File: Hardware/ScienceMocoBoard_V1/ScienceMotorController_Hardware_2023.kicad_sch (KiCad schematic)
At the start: 134 parts, among them Q1 SI4156DY, Q10 SI4156DY, Q11 SI4156DY, Q12 SI4156DY, Q13 SI4156DY, Q14 SI4156DY, Q15 SI4156DY, Q16 SI4156DY, Q2 SI4156DY, Q3 SI4156DY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

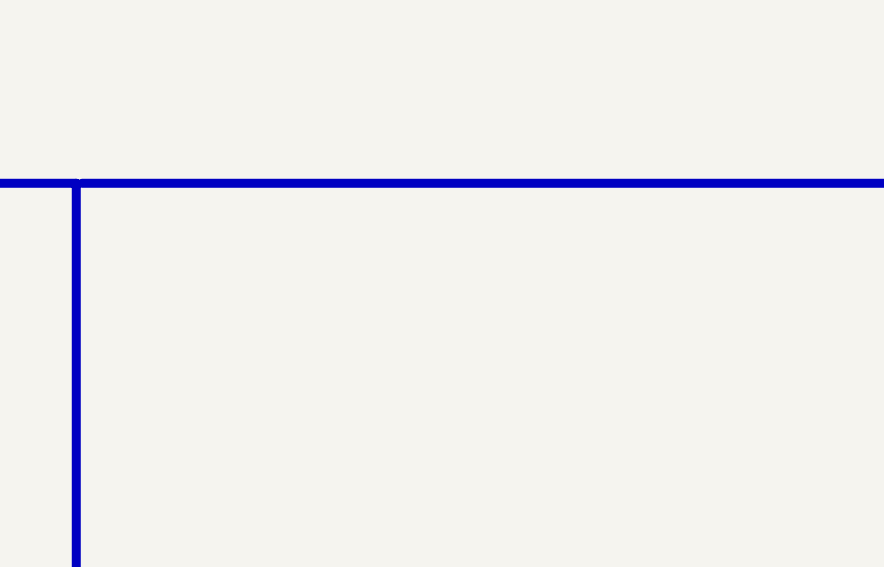
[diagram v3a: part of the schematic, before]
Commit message: Added Mounting Holes
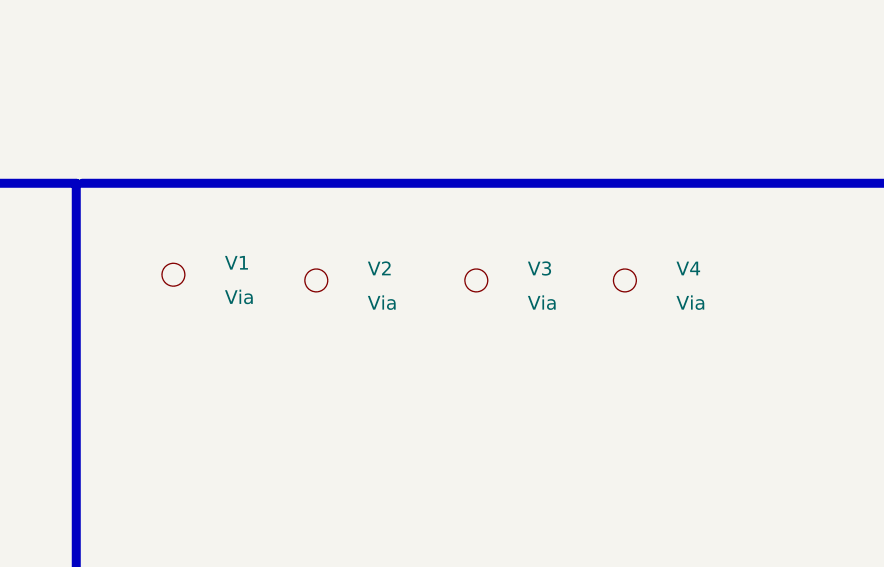
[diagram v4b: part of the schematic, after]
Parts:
- added V1, V2, V3, V4: Via, MRDT_Drill_Holes:4_40_Hole_Corner, symbol MRDT_Drill_Holes:Via
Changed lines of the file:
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@@
     (pin "8")
   )
+  (symbol (lib_id "MRDT_Drill_Holes:Via") (at 377.19 262.255 0) (unit 1)
+    (in_bom yes) (on_board yes) (fields_autoplaced)
+    (property "Reference" "V4" (id 0) (at 382.905 260.985 0)
+      (effects (font (size 1.524 1.524)) (justify left))
+    )
+    (property "Value" "Via" (id 1) (at 382.905 264.795 0)
+      (effects (font (size 1.524 1.524)) (justify left))
+    )
+    (property "Footprint" "MRDT_Drill_Holes:4_40_Hole_Corner" (id 2) (at 377.19 262.255 0)
+      (effects (font (size 1.524 1.524)) hide)
+    )
+    (property "Datasheet" "" (id 3) (at 377.19 262.255 0)
+      (effects (font (size 1.524 1.524)) hide)
+    )
+    (pin "1")
+  )
   (symbol (lib_id "MRDT_Devices:OKI") (at 88.9 300.355 0) (unit 1)
     (in_bom yes) (on_board yes)
@@
     (pin "1")
   )
+  (symbol (lib_id "MRDT_Drill_Holes:Via") (at 327.025 261.62 0) (unit 1)
+    (in_bom yes) (on_board yes) (fields_autoplaced)
+    (property "Reference" "V1" (id 0) (at 332.74 260.35 0)
+      (effects (font (size 1.524 1.524)) (justify left))
+    )
+    (property "Value" "Via" (id 1) (at 332.74 264.16 0)
+      (effects (font (size 1.524 1.524)) (justify left))
+    )
+    (property "Footprint" "MRDT_Drill_Holes:4_40_Hole_Corner" (id 2) (at 327.025 261.62 0)
+      (effects (font (size 1.524 1.524)) hide)
+    )
+    (property "Datasheet" "" (id 3) (at 327.025 261.62 0)
+      (effects (font (size 1.524 1.524)) hide)
+    )
+    (pin "1")
+  )
   (symbol (lib_id "Device:R") (at 93.98 105.41 90) (unit 1)
     (in_bom yes) (on_board yes)
@@
     (pin "2")
   )
+  (symbol (lib_id "MRDT_Drill_Holes:Via") (at 342.9 262.255 0) (unit 1)
+    (in_bom yes) (on_board yes) (fields_autoplaced)
+    (property "Reference" "V2" (id 0) (at 348.615 260.985 0)
+      (effects (font (size 1.524 1.524)) (justify left))
+    )
+    (property "Value" "Via" (id 1) (at 348.615 264.795 0)
+      (effects (font (size 1.524 1.524)) (justify left))
+    )
+    (property "Footprint" "MRDT_Drill_Holes:4_40_Hole_Corner" (id 2) (at 342.9 262.255 0)
+      (effects (font (size 1.524 1.524)) hide)
+    )
+    (property "Datasheet" "" (id 3) (at 342.9 262.255 0)
+      (effects (font (size 1.524 1.524)) hide)
+    )
+    (pin "1")
+  )
   (symbol (lib_id "Simulation_SPICE:DIODE") (at 46.99 191.77 270) (unit 1)
     (in_bom yes) (on_board yes) (fields_autoplaced)
@@
     (pin "1")
   )
+  (symbol (lib_id "MRDT_Drill_Holes:Via") (at 360.68 262.255 0) (unit 1)
+    (in_bom yes) (on_board yes) (fields_autoplaced)
+    (property "Reference" "V3" (id 0) (at 366.395 260.985 0)
+      (effects (font (size 1.524 1.524)) (justify left))
+    )
+    (property "Value" "Via" (id 1) (at 366.395 264.795 0)
+      (effects (font (size 1.524 1.524)) (justify left))
+    )
+    (property "Footprint" "MRDT_Drill_Holes:4_40_Hole_Corner" (id 2) (at 360.68 262.255 0)
+      (effects (font (size 1.524 1.524)) hide)
+    )
+    (property "Datasheet" "" (id 3) (at 360.68 262.255 0)
+      (effects (font (size 1.524 1.524)) hide)
+    )
+    (pin "1")
+  )
   (symbol (lib_id "power:GND") (at 110.49 199.39 0) (unit 1)
     (in_bom yes) (on_board yes) (fields_autoplaced)
@@
       (reference "U11") (unit 8) (value "TM4C129E_Launchpad") (footprint "MRDT_Shields:TM4C129E_Launchpad_FULL_THT_BOTTOM")
     )
+    (path "/385e1073-e8ee-4204-8262-b68e828176b6"
+      (reference "V1") (unit 1) (value "Via") (footprint "MRDT_Drill_Holes:4_40_Hole_Corner")
+    )
+    (path "/b4dcbca0-27b8-40c0-8259-04e5ea35a88a"
+      (reference "V2") (unit 1) (value "Via") (footprint "MRDT_Drill_Holes:4_40_Hole_Corner")
+    )
+    (path "/df564af1-db08-44de-89e6-2a6bfacb7389"
+      (reference "V3") (unit 1) (value "Via") (footprint "MRDT_Drill_Holes:4_40_Hole_Corner")
+    )
+    (path "/2c35478b-bc32-43b3-89fb-253ddd3b5959"
+      (reference "V4") (unit 1) (value "Via") (footprint "MRDT_Drill_Holes:4_40_Hole_Corner")
+    )
   )

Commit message: Stuff Happened
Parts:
- C11, C12, C5, C6: value 10u -> 10uF
- R11, R16, R17, R18, R19, R32, R33, R34, R35, R36, R37, R38, R39: value 130 -> 120

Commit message: Updated to Teensy.
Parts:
- removed D24, D25: RED, LED_SMD:LED_0603_1608Metric_Pad1.05x0.95mm_HandSolder, symbol Device:LED_Small
- removed R32, R33: 120, Resistor_SMD:R_0603_1608Metric_Pad0.98x0.95mm_HandSolder, symbol Device:R
- removed U11: TM4C129E_Launchpad, MRDT_Shields:TM4C129E_Launchpad_FULL_THT_BOTTOM, symbol MRDT_Shields:TM4C129E_Launchpad
- added U11: Teensy4.1_DEV-16771, MRDT_Shields:Teensy_4_1, symbol MRDT_Shields:Teensy4.1_DEV-16771
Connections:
- new net: U11.3.3V_1 (3.3V), U11.3.3V_2 (3.3V), U11.3.3V_3 (3.3V)
- new net: U11.GND1 (GND), U11.GND2 (GND), U11.GND3 (GND), U11.GND4 (GND), U11.GND5 (GND)
- new net: U11.USB_GND1 (USB_GND), U11.USB_GND2 (USB_GND)
- no-connect marks 48 -> 0
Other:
- note added: "TEENSY"
- note removed: "Red"
- note removed: "TIVA"

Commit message: Added Ethernet. Expanded Board Temporarily
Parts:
- added C15: 0.1uF, Capacitor_SMD:C_0603_1608Metric_Pad1.08x0.95mm_HandSolder, symbol Device:C
- added D24: YELLOW, LED_SMD:LED_0603_1608Metric_Pad1.05x0.95mm_HandSolder, symbol Device:LED_Small
- added J1: RJ45_LED_Shielded, MRDT_Connectors:RJ45_Teensy, symbol Connector:RJ45_LED_Shielded
- added J2: Conn_02x03_Counter_Clockwise, Connector_PinHeader_2.00mm:PinHeader_2x03_P2.00mm_Vertical, symbol Connector_Generic:Conn_02x03_Counter_Clockwise
- added LimSwitch7: Molex_SL_02, MRDT_Connectors:MOLEX_SL_02_Vertical, symbol MRDT_Connectors:Molex_SL_02
- added R32: 120, Resistor_SMD:R_0603_1608Metric_Pad0.98x0.95mm_HandSolder, symbol Device:R
- C10, C13, C14, C2, C3, C7, C8, C9: value 0.1u -> 1uF
- renumbered LimSwitch3 to LimSwitch1, LimSwitch1 to LimSwitch2, LimSwitch2 to LimSwitch3
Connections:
- net +3V3: now also LimSwitch7.1
- net Encoder_PWM_1: now also U11.38 (A14)
- net Encoder_PWM_2: now also U11.39 (A15)
- net Encoder_PWM_3: now also U11.40 (A16)
- net Encoder_PWM_4: now also U11.41 (A17)
- net FWD_PWM_1: now also U11.1 (TX1)
- net FWD_PWM_2: now also U11.3 (LRCLK2)
- net FWD_PWM_3: now also U11.6 (OUT1D)
- net FWD_PWM_4: now also U11.8 (TX2)
- net GND: now also U11.GND1 (GND), U11.GND2 (GND), U11.GND3 (GND), U11.GND4 (GND), U11.GND5 (GND), D24.1 (K), J1.SH
- net Limit_Switch_1: now also U11.16 (A2)
- net Limit_Switch_2: now also U11.17 (A3)
- net Limit_Switch_3: now also U11.18 (A4)
- net Limit_Switch_4: now also U11.19 (A5)
- net Limit_Switch_5: now also U11.20 (A6)
- net Limit_Switch_6: now also U11.21 (A7)
- net RVS_PWM_1: now also U11.2 (OUT2)
- net RVS_PWM_2: now also U11.4 (BCLK2)
- net RVS_PWM_3: now also U11.7 (RX2)
- net RVS_PWM_4: now also U11.9 (OUT1C)
- net Servo_1: now also U11.37 (CS3)
- net Servo_2: now also U11.36 (CS2)
- net Servo_3: now also U11.12 (MISO)
- net Servo_4: now also U11.11 (MOSI)
- net Servo_5: now also U11.24 (A10)
- net Servo_6: now also U11.23 (A9)
- net Limit_Switch_7: now reaches U11.22 (A8)
- net Limit_Switch_7: now also LimSwitch7.2, R32.2
- net +3.3V: now reaches U11.3.3V_1 (3.3V), U11.3.3V_2 (3.3V), U11.3.3V_3 (3.3V)
- new net: C15.1, J1.2, J1.5
- new net: C15.2, J1.8
- new net: D24.2 (A), R32.1
- new net: J1.1, J2.1 (Pin_1)
- new net: J1.10, J2.4 (Pin_4)
- new net: J1.3, J2.2 (Pin_2)
- new net: J1.4, J2.6 (Pin_6)
- new net: J1.6, J2.5 (Pin_5)
- new net: J1.9, J2.3 (Pin_3)
- no-connect marks 0 -> 33
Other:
- note added: "Rx +"
- note added: "Rx -"
- note added: "Tx +"
- note added: "Tx -"
- note added: "Vias"
- moved on the sheet: U11, V1, V2, V3, V4

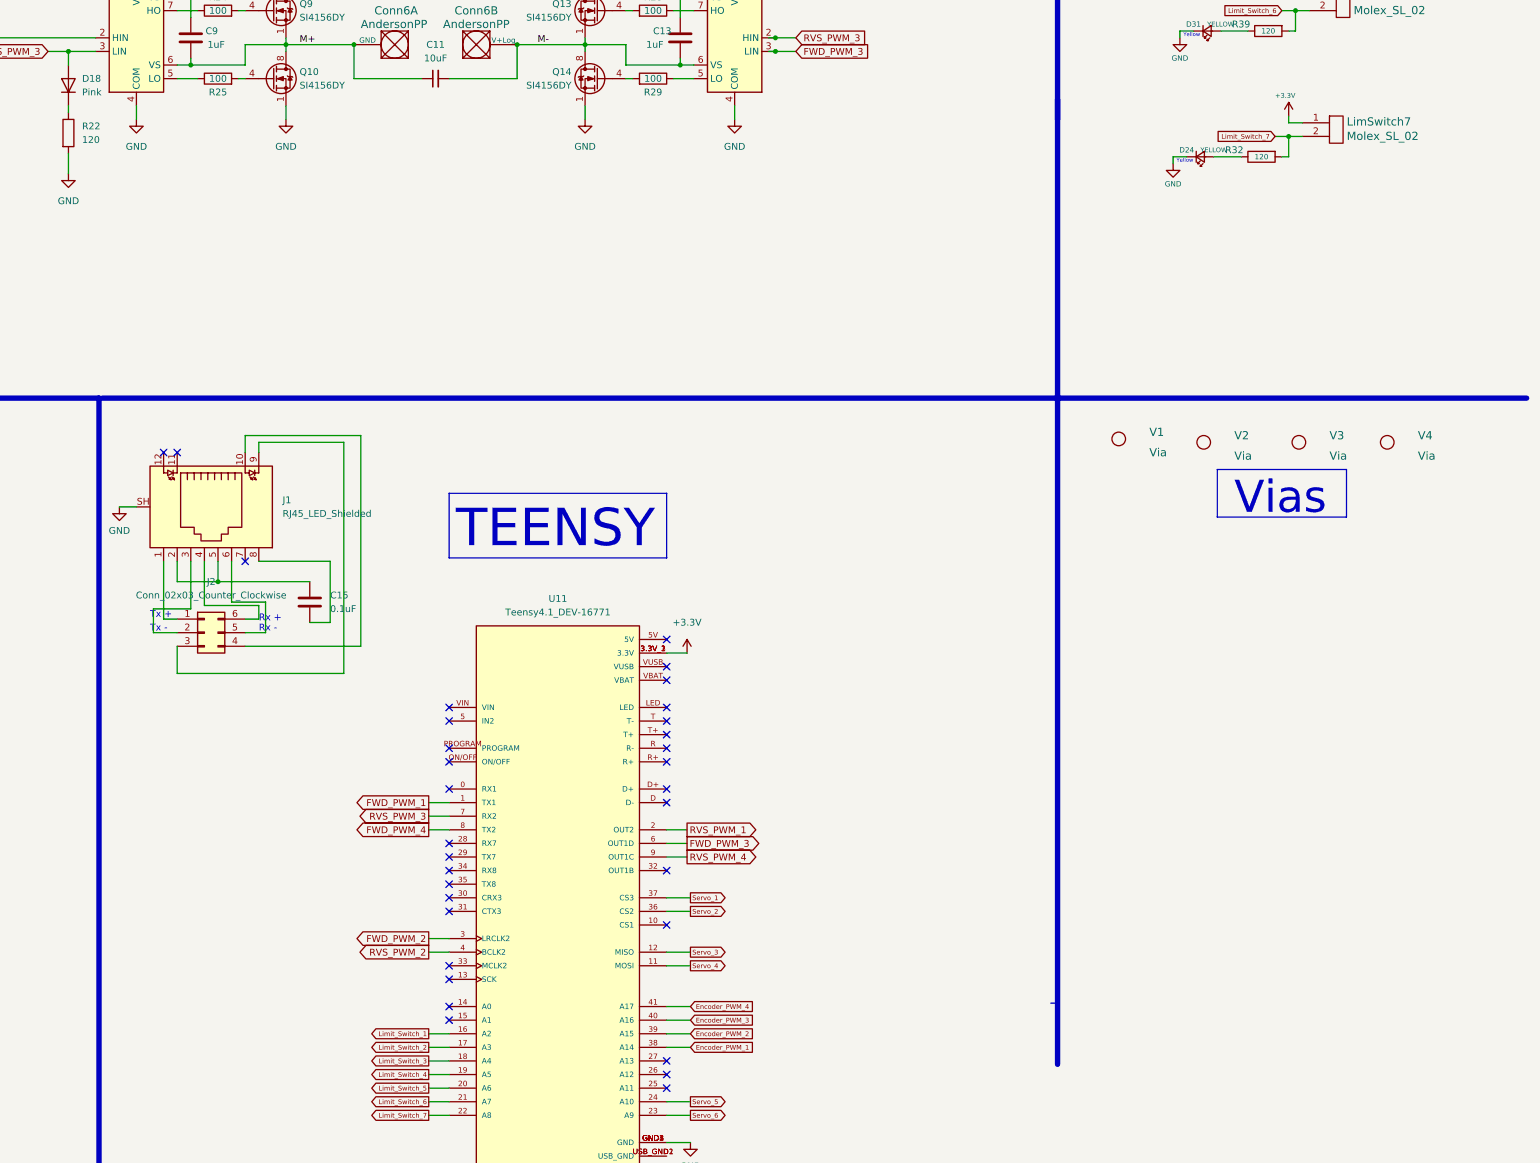
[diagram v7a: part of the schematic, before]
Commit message: Added Buttons to Schematic.
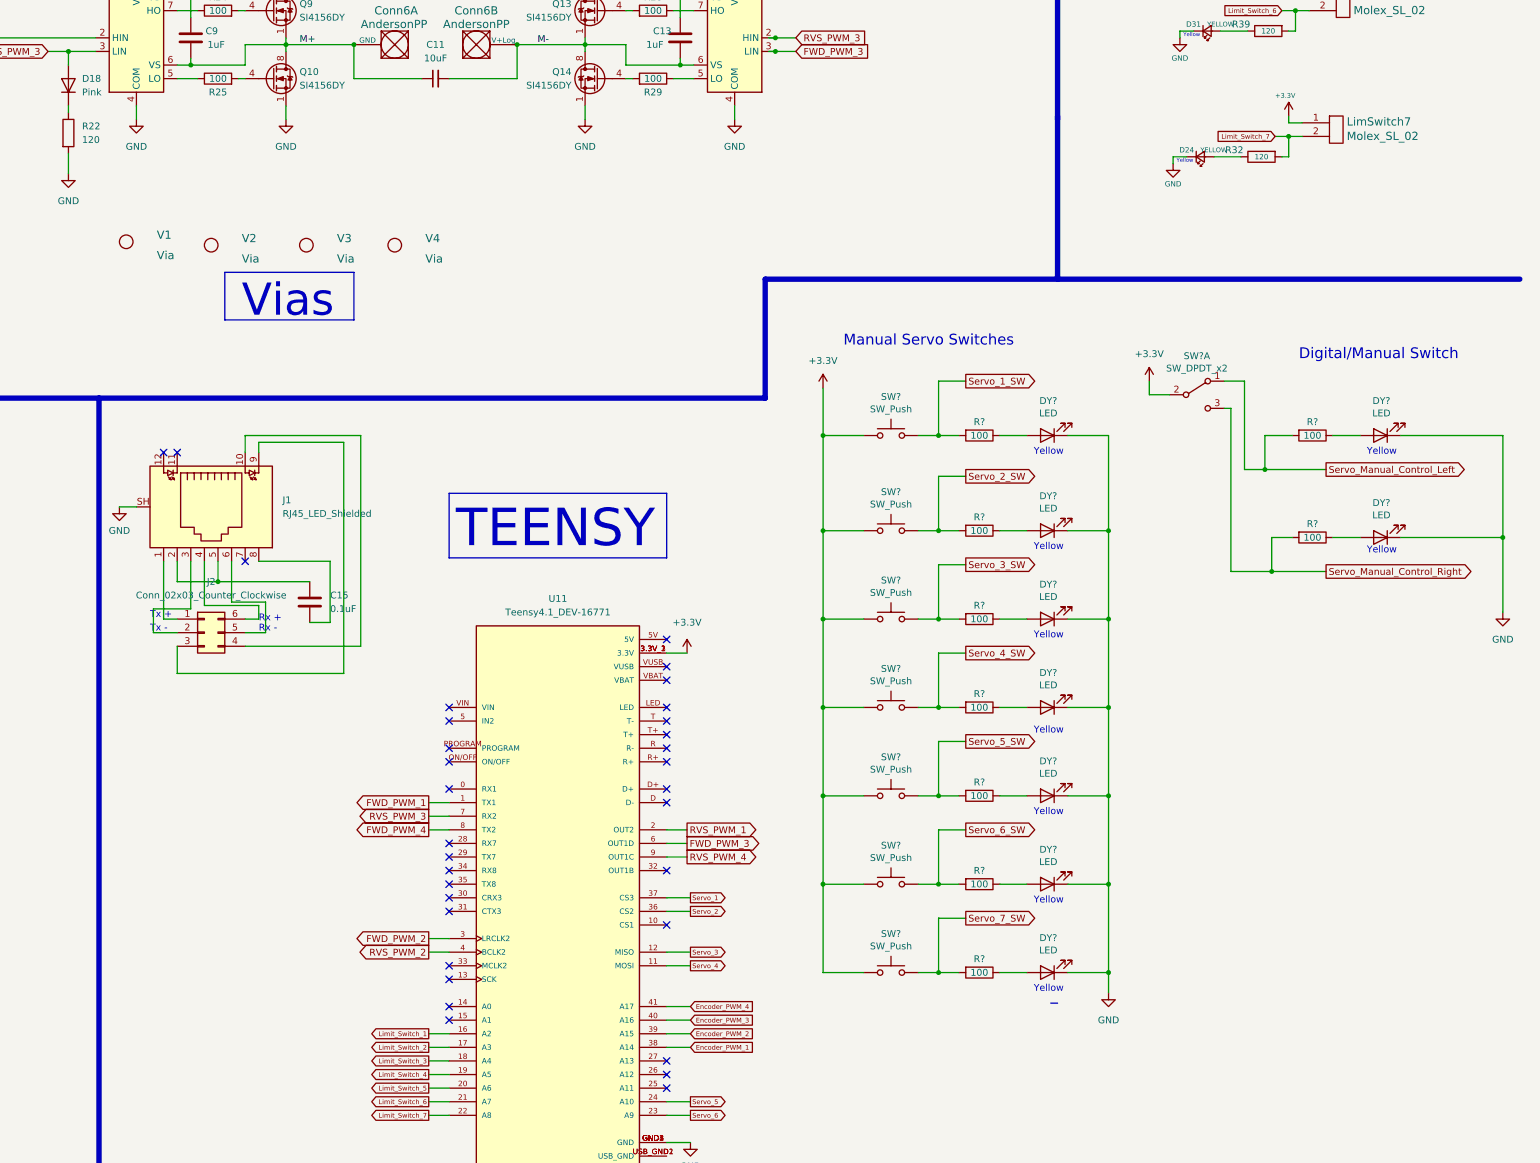
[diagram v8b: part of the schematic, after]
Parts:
- added DY? (x9): LED, LED_SMD:LED_0603_1608Metric_Pad1.05x0.95mm_HandSolder, symbol Device:LED
- added R? (x9): 100, Resistor_SMD:R_0603_1608Metric_Pad0.98x0.95mm_HandSolder, symbol Device:R
- added SW? (x7): SW_Push, Button_Switch_SMD:SW_SPST_EVPBF, symbol Switch:SW_Push
- added SW?: SW_DPDT_x2, Button_Switch_THT:SW_Slide_1P2T_CK_OS102011MS2Q, symbol Switch:SW_DPDT_x2
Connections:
- net +3.3V: now also SW?.1, SW?.1, SW?.1, SW?.1, SW?.1, SW?.1, SW?.2, SW?.2 (B)
- net GND: now also DY?.1 (K), DY?.1 (K), DY?.1 (K), DY?.1 (K), DY?.1 (K), DY?.1 (K), DY?.1 (K), DY?.1 (K), DY?.1 (K)
- new net: DY?.2 (A), R?.1 (x9)
- new net Servo_1_SW: R?.2, SW?.1
- new net Servo_2_SW: R?.2, SW?.2
- new net Servo_3_SW: R?.2, SW?.2
- new net Servo_4_SW: R?.2, SW?.2
- new net Servo_5_SW: R?.2, SW?.2
- new net Servo_6_SW: R?.2, SW?.2
- new net Servo_7_SW: R?.2, SW?.2
- new net Servo_Manual_Control_Left: R?.2, SW?.1 (A)
- new net Servo_Manual_Control_Right: R?.2, SW?.3 (C)
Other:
- note added: "Digital/Manual Switch"
- note added: "Manual Servo Switches"
- moved on the sheet: V1, V2, V3, V4
